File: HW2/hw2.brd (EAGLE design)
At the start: 50 x 50 mm, 23 parts, among them J1 USB-MINIB-5PUSB-MINIB-2SUPPORT, SW3 1825232-1PUSH_BUTTON_2SUPPORT

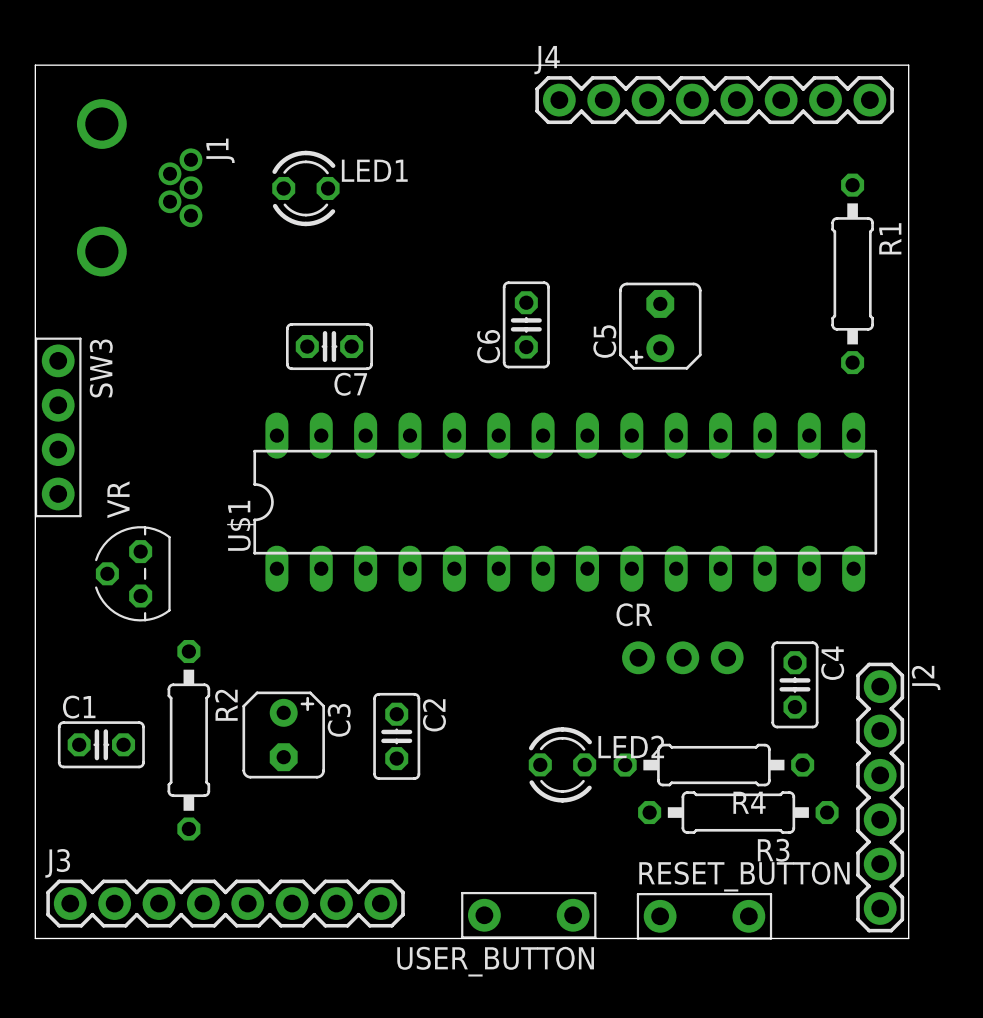
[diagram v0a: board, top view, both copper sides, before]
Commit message: Board layout drawn, top and bottom
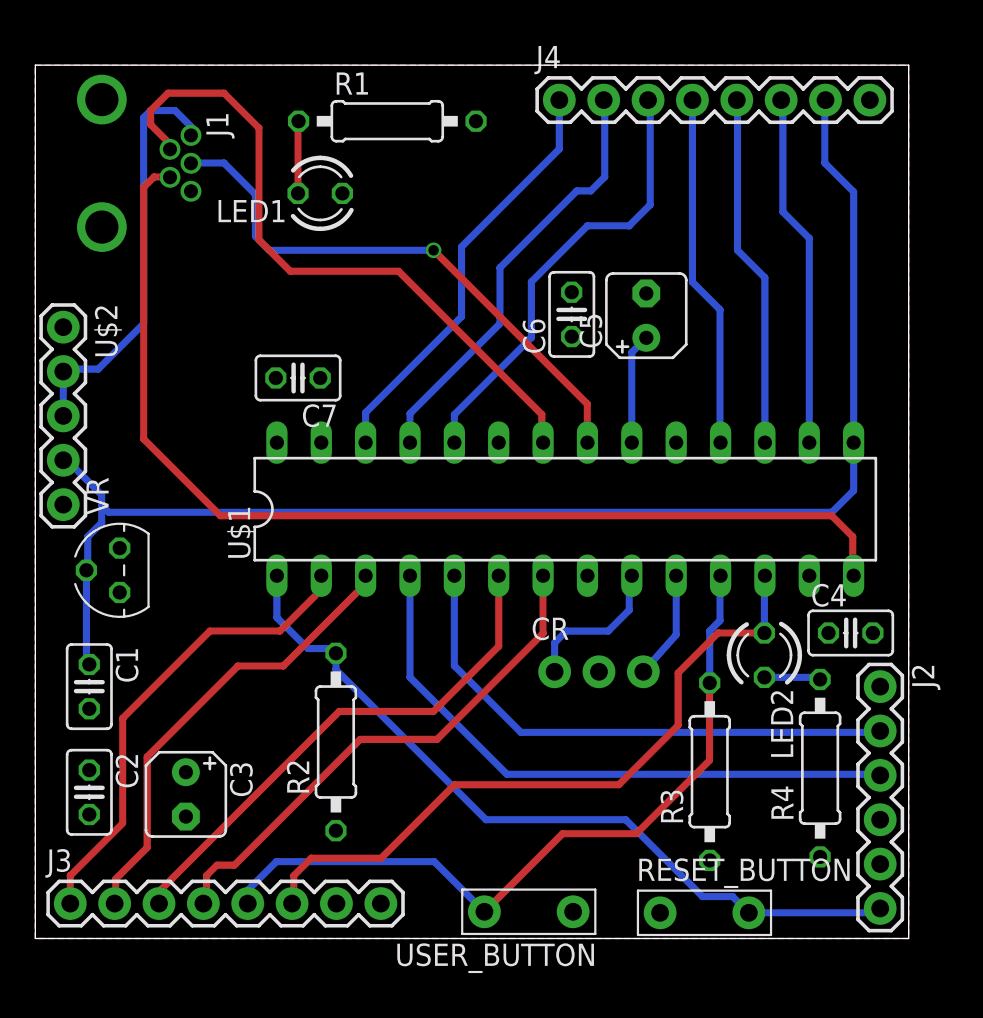
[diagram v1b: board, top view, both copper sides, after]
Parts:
- removed SW3: 1825232-1PUSH_BUTTON_2SUPPORT, hw2:1X04_NO_SILK_ALL_ROUND_BOUNDED
- added U$2: 1825232-1, hw2:1X05
- J2: value (none) -> M06
- J3: value (none) -> M08_1
- J4: value (none) -> M08_2
- moved R1 28.0 mm to (20.1, 46.8), turned to 0 degrees
- moved C2 17.9 mm to (3.09, 8.37)
- moved LED2 13.2 mm to (41.7, 16.2), turned to 270 degrees
- moved R2 8.42 mm to (17.2, 11.2), turned to 90 degrees
- moved C3 6.55 mm to (8.62, 8.25)
- moved R4 6.08 mm to (44.9, 9.75), turned to 90 degrees
- moved CR 4.87 mm to (29.7, 15.3)
- moved C4 4.36 mm to (46.7, 17.5), turned to 0 degrees
- moved C1 3.40 mm to (3.09, 14.4), turned to 270 degrees
- moved R3 2.86 mm to (38.6, 9.55), turned to 90 degrees
- moved C6 2.67 mm to (30.7, 35.7)
- moved C7 2.55 mm to (15.0, 32.1)
- moved J1 1.40 mm to (3.81, 44.4)
- moved VR 1.22 mm to (4.83, 21.1)
- moved C5 1.00 mm to (35.0, 35.7)
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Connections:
- net +5V: now also U$2.4; no longer SW3.4
- net N$4: now also U$2.2, U$2.3; no longer SW3.1
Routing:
- net +5V: track 0.00 -> 79.9 mm
- net N$1: track 0.00 -> 61.3 mm
- net N$7: track 0.00 -> 44.6 mm
- net N$10: track 0.00 -> 43.9 mm
- net N$12: track 0.00 -> 39.5 mm
- net N$5: track 0.00 -> 38.5 mm
- net N$8: track 0.00 -> 35.1 mm
- net N$2: track 0.00 -> 32.0 mm, vias 0 -> 1
- net N$6: track 0.00 -> 31.2 mm
- net N$17: track 0.00 -> 30.9 mm
- net N$18: track 0.00 -> 30.0 mm
- net N$16: track 0.00 -> 27.3 mm
- net N$15: track 0.00 -> 27.1 mm
- net N$21: track 0.00 -> 25.7 mm
- net N$20: track 0.00 -> 24.7 mm
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- added copper zone on layer 1, net +3V3
- added copper zone on layer 16, net GND
